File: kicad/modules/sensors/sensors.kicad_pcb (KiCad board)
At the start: 2 copper layers, 84.6 x 64 mm, 46 parts, among them J1 Bus_PCI_Express_x1, J2 TYPE-C-31-M-04, J3 Conn_01x02, U2 RP2040, U4 W25Q128JVP, U5 BMP388, U8 BNO055, U9 MCP25625T-E/ML, X1 ABM8-272-T3, Y1 ABS07-32.768KHZ-T, Y2 X322516MLB4SI

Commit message: begin routing
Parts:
- removed J3: Conn_01x02, Connector_PinHeader_2.54mm:PinHeader_1x02_P2.54mm_Vertical
- added J4: Conn_01x02, Connector_PinHeader_2.54mm:PinHeader_1x02_P2.54mm_Vertical, F.Cu at (122.0, 116.7)
- moved C10 93.2 mm to (148.5, 91.0)
- moved R12 91.0 mm to (146.3, 92.1), turned to 90 degrees
- moved C11 89.8 mm to (145.0, 90.5), turned to 180 degrees
- moved C207 80.9 mm to (59.5, 86.9)
- moved R220 76.9 mm to (59.5, 98.9)
- moved R221 76.9 mm to (59.5, 100.9)
- moved C211 73.1 mm to (59.5, 90.0)
- moved C212 73.1 mm to (59.5, 92.0)
- moved C213 73.1 mm to (59.5, 93.9)
- moved C214 73.1 mm to (59.5, 95.9)
- moved S1 55.7 mm to (161.0, 117.4), turned to 180 degrees
- moved S2 35.9 mm to (131.0, 117.0), turned to 180 degrees
- moved R203 34.7 mm to (146.0, 105.5), turned to 90 degrees
- moved R204 31.9 mm to (144.5, 105.5), turned to 90 degrees
- moved C210 30.7 mm to (142.0, 105.5), turned to -90 degrees
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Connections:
- net Net-(C11-Pad1) renamed /XOUT_pre
- S1 pad A: Net-(S1-PadA) -> GND
- S1 pad B: Net-(S1-PadA) -> GND
- S1 pad C: Net-(S1-PadC) -> /~{USB_BOOT_S}
- S1 pad D: Net-(S1-PadC) -> /~{USB_BOOT_S}
- S2 pad A: Net-(S2-PadA) -> GND
- S2 pad B: Net-(S2-PadA) -> GND
- S2 pad C: Net-(S2-PadC) -> /RUN
- S2 pad D: Net-(S2-PadC) -> /RUN
- U2 pad 24: unconnected-(U2-SWCLK-Pad24) -> /SWCLK
- U2 pad 25: unconnected-(U2-SWD-Pad25) -> /SWD
- U2 pad 26: unconnected-(U2-RUN-Pad26) -> /RUN
- U2 pad 51: unconnected-(U2-QSPI_SD3-Pad51) -> /QSPI_SD3
- U2 pad 53: unconnected-(U2-QSPI_SD0-Pad53) -> /QSPI_SD0
- U2 pad 54: unconnected-(U2-QSPI_SD2-Pad54) -> /QSPI_SD2
- U2 pad 55: unconnected-(U2-QSPI_SD1-Pad55) -> /QSPI_SD1
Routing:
- net /QSPI_SS: track 0.00 -> 19.6 mm
- net /QSPI_SD1: track 0.00 -> 17.0 mm
- net /QSPI_SD2: track 0.00 -> 15.5 mm
- net /XIN: track 0.00 -> 8.78 mm
- net +3.3V: track 0.00 -> 8.31 mm
- net /QSPI_SD3: track 0.00 -> 8.02 mm
- net +1.1V: track 0.00 -> 7.47 mm
- net /QSPI_SCLK: track 0.00 -> 7.09 mm
- net /QSPI_SD0: track 0.00 -> 6.17 mm
- net /XOUT_pre: track 0.00 -> 3.10 mm
- net /XOUT: track 0.00 -> 1.70 mm

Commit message: continue routing
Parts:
- moved R220 103.5 mm to (163.0, 100.5), turned to 180 degrees
- moved R221 93.5 mm to (153.0, 99.5), turned to 180 degrees
- moved C81 87.4 mm to (167.6, 88.1)
- moved C50 86.3 mm to (160.0, 97.0)
- moved C51 83.3 mm to (157.0, 98.5), turned to 180 degrees
- moved C82 82.6 mm to (162.6, 88.1)
- moved R87 80.6 mm to (159.0, 87.5), turned to 90 degrees
- moved C84 78.0 mm to (158.0, 91.0)
- moved D88 76.0 mm to (155.5, 92.5)
- moved R89 73.8 mm to (153.8, 94.0), turned to 180 degrees
- moved R83 72.7 mm to (153.1, 97.3), turned to 90 degrees
- moved Y1 50.0 mm to (169.7, 92.1)
- moved U8 37.3 mm to (162.8, 92.4), turned to -90 degrees
- moved U5 32.3 mm to (159.7, 99.0)
- moved Y2 31.5 mm to (139.2, 79.4), turned to 180 degrees
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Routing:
- net SDA: track 0.00 -> 22.1 mm
- net SCL: track 0.00 -> 21.6 mm
- net BOOT_LOAD: track 0.00 -> 19.7 mm
- net SO: track 0.00 -> 16.4 mm
- net BNORESET: track 0.00 -> 13.3 mm
- net BNOINT: track 0.00 -> 12.8 mm
- net +3.3V: track 8.31 -> 15.6 mm
- net OSC2: track 0.00 -> 6.82 mm
- net Net-(U8-XOUT32): track 0.00 -> 6.05 mm
- net Net-(U8-XIN32): track 0.00 -> 5.43 mm
- net Net-(D88-A): track 0.00 -> 4.95 mm
- net OSC1: track 0.00 -> 4.47 mm
- net Net-(U8-CAP): track 0.00 -> 2.87 mm
- net Net-(D88-K): track 0.00 -> 1.53 mm
- net /XOUT: track 1.70 -> 2.79 mm
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
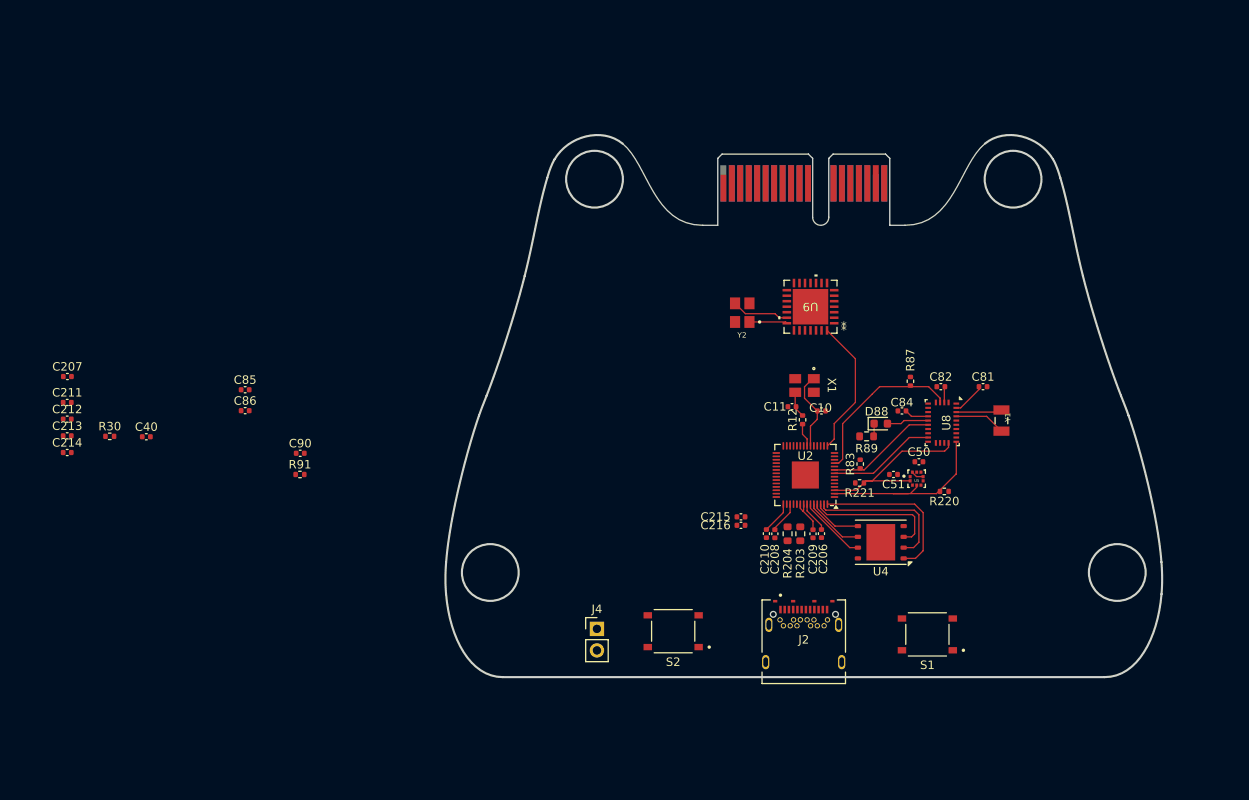
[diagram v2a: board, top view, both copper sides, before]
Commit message: finish most routing
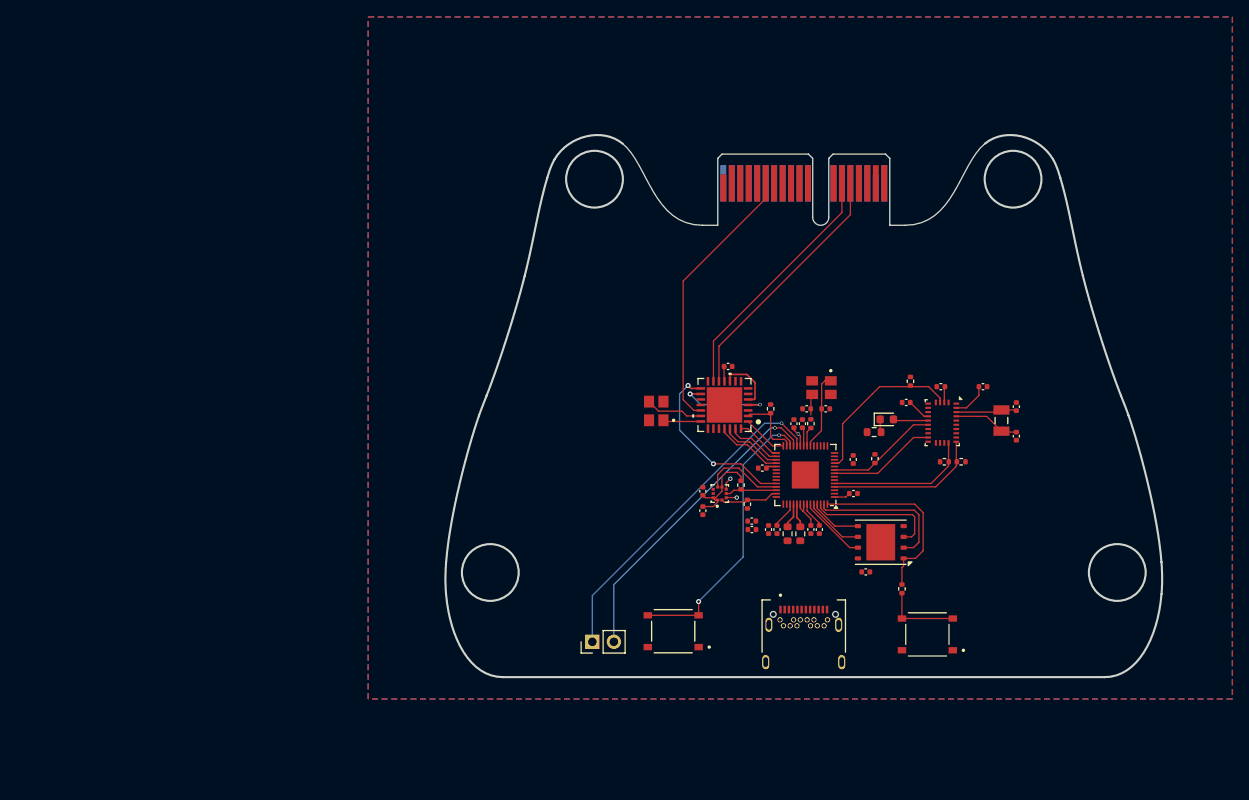
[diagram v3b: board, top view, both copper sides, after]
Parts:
- added R222: 4.7k, Resistor_SMD:R_0402_1005Metric, F.Cu at (139.8, 102.0)
- added R223: 4.7k, Resistor_SMD:R_0402_1005Metric, F.Cu at (139.0, 99.8)
- X1: footprint crystal:ABM8-272-T3_ABR -> ABM8-272-T3:ABM8-272-T3_ABR
- moved R30 95.2 mm to (158.0, 112.0), turned to -90 degrees
- moved C211 93.4 mm to (152.3, 100.8)
- moved C213 92.8 mm to (152.2, 96.7), turned to 90 degrees
- moved C85 91.2 mm to (171.5, 94.0), turned to -90 degrees
- moved C86 91.0 mm to (171.5, 90.5), turned to -90 degrees
- moved C214 86.8 mm to (146.2, 92.5), turned to 90 degrees
- moved C40 86.4 mm to (153.7, 110.0)
- moved C207 85.9 mm to (145.2, 92.5), turned to 90 degrees
- moved C212 82.2 mm to (141.5, 97.8), turned to 180 degrees
- moved R91 56.1 mm to (142.5, 90.8), turned to -90 degrees
- moved C90 51.5 mm to (137.5, 85.8)
- moved C50 26.1 mm to (134.5, 102.8), turned to -90 degrees
- moved U5 23.3 mm to (136.5, 100.8), turned to 90 degrees
- moved C51 22.6 mm to (134.5, 100.5), turned to 90 degrees
- moved Y2 15.4 mm to (129.0, 91.0)
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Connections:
- J1 pad A13: CANL -> CANH
- J1 pad A14: CANH -> CANL
- J1 pad B13: CANL -> CANH
- J1 pad B14: CANH -> CANL
- J2 pad A6: UDB_D+ -> USB_D+
- J2 pad A7: UDB_D- -> USB_D-
- J2 pad B6: UDB_D+ -> USB_D+
- J2 pad B7: UDB_D- -> USB_D-
- R203 pad 1: /USB_D+ -> USB_D+
- R204 pad 1: /USB_D- -> USB_D-
- R220 pad 1: +3V3 -> +3.3V
- R220 pad 2: SDA -> SDA1
- R221 pad 1: SCL -> SCL1
- R221 pad 2: +3V3 -> +3.3V
- U2 pad 14: SI -> unconnected-(U2-GPIO11-Pad14)
- U2 pad 15: SO -> unconnected-(U2-GPIO12-Pad15)
- U2 pad 16: CS -> unconnected-(U2-GPIO13-Pad16)
- U2 pad 17: SCK -> unconnected-(U2-GPIO14-Pad17)
- U2 pad 2: SDA -> unconnected-(U2-GPIO0-Pad2)
- U2 pad 27: CANSTBY -> CANRESET
- U2 pad 28: CANINT -> CS
- U2 pad 29: unconnected-(U2-GPIO18-Pad29) -> SO
- U2 pad 3: SCL -> unconnected-(U2-GPIO1-Pad3)
- U2 pad 30: unconnected-(U2-GPIO19-Pad30) -> SI
- U2 pad 31: unconnected-(U2-GPIO20-Pad31) -> SCK
- U2 pad 32: unconnected-(U2-GPIO21-Pad32) -> CANINT
- U2 pad 38: unconnected-(U2-GPIO26_ADC0-Pad38) -> CANSTBY
- U2 pad 39: unconnected-(U2-GPIO27_ADC1-Pad39) -> BMPINT
- U2 pad 4: unconnected-(U2-GPIO2-Pad4) -> SDA1
- U2 pad 40: unconnected-(U2-GPIO28_ADC2-Pad40) -> SDA0
- U2 pad 41: unconnected-(U2-GPIO29_ADC3-Pad41) -> SCL0
- U2 pad 5: BMPINT -> SCL1
- U5 pad 2: SCL -> SCL0
- U5 pad 4: SDA -> SDA0
- U8 pad 19: SCL -> SCL1
- U8 pad 20: SDA -> SDA1
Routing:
- net /SWCLK: track 0.00 -> 39.6 mm, vias 0 -> 1
- net /SWD: track 0.00 -> 36.9 mm, vias 0 -> 1
- net /RUN: track 0.00 -> 33.8 mm, vias 0 -> 2
- net +5V: track 0.00 -> 32.2 mm
- net CANL: track 0.00 -> 29.8 mm
- net CANH: track 0.00 -> 29.6 mm
- net SDA: track 22.1 -> 0.00 mm
- net SCL: track 21.6 -> 0.00 mm
- net CANSTBY: track 0.00 -> 21.3 mm, vias 0 -> 2
- net SDA1: track 0.00 -> 18.3 mm
- net SCL1: track 0.00 -> 17.0 mm
- net +3.3V: track 15.6 -> 27.8 mm
- net tx: track 0.00 -> 11.5 mm, vias 0 -> 2
- net SO: track 16.4 -> 5.35 mm
- net BMPINT: track 0.00 -> 9.62 mm
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- added copper zone on B.Cu, net GND
- added copper zone on F.Cu, net GND

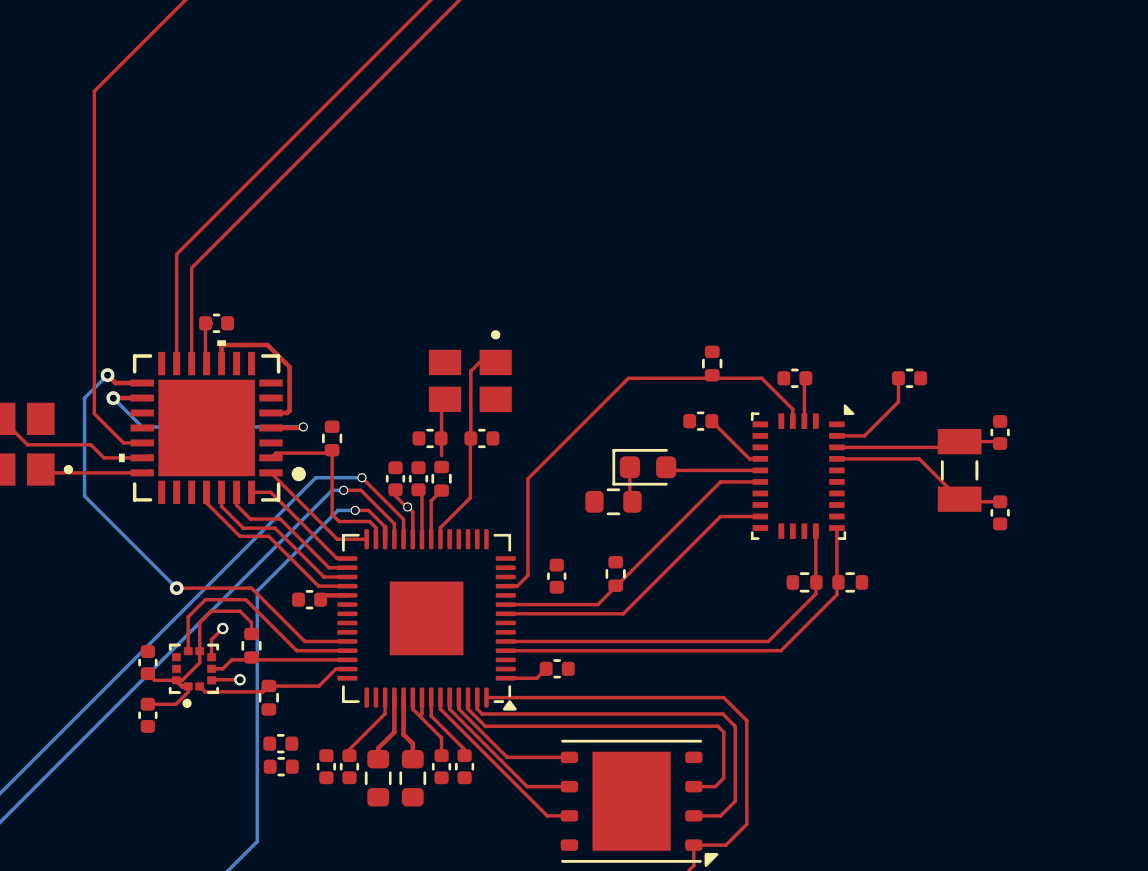
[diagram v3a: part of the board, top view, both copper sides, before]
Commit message: add new sensors, LDO and MOSFET
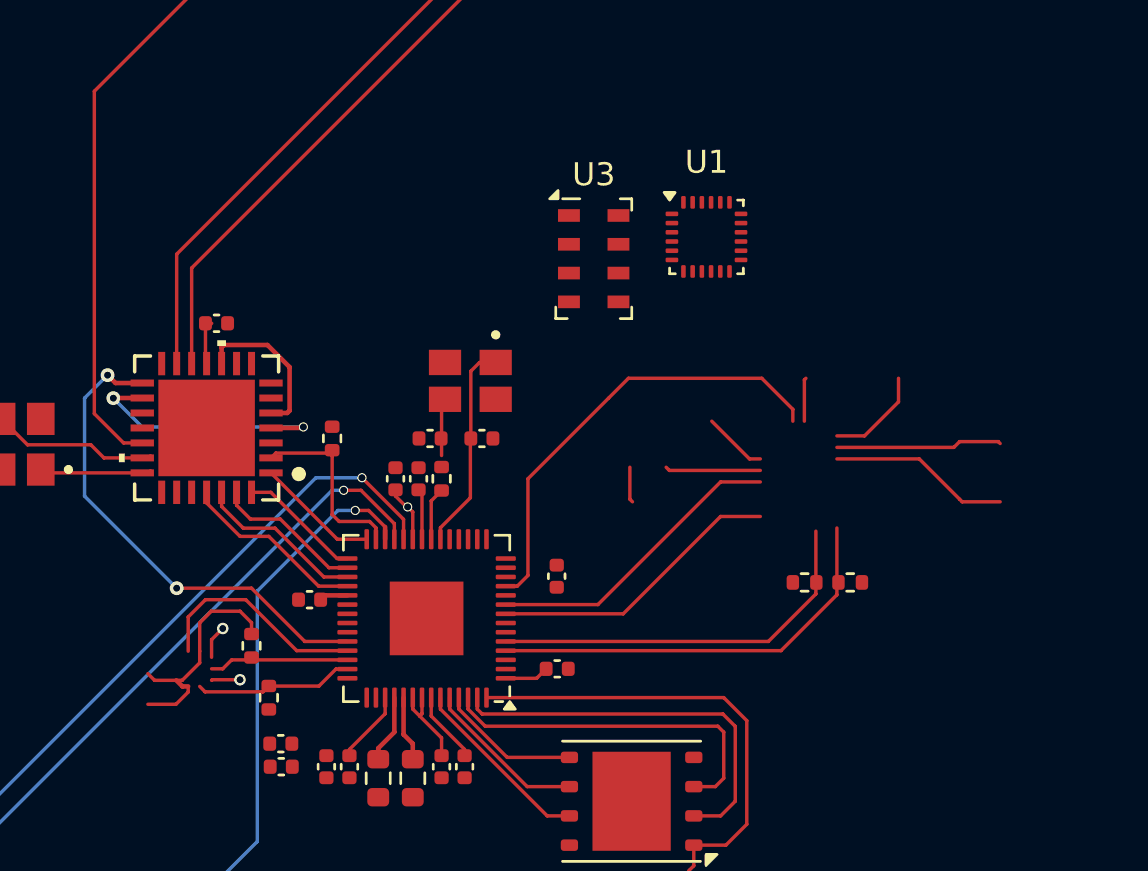
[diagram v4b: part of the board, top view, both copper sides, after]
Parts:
- removed C50, C51, C81, C82: 100n, Capacitor_SMD:C_0402_1005Metric
- removed C84: 1u, Capacitor_SMD:C_0402_1005Metric
- removed C85, C86: 22p, Capacitor_SMD:C_0402_1005Metric
- removed D88: LED, LED_SMD:LED_0603_1608Metric
- removed R83, R87: 10k, Resistor_SMD:R_0402_1005Metric
- removed R89: 150, Resistor_SMD:R_0603_1608Metric
- removed U5: BMP388, BMP388:PQFN50P200X200X80-10N
- removed U8: BNO055, Package_LGA:LGA-28_5.2x3.8mm_P0.5mm
- removed Y1: ABS07-32.768KHZ-T, ABS07-32.768KHZ-T:XTAL_ABS07-32.768KHZ-T
- added U1: ICM-20948, Sensor_Motion:InvenSense_QFN-24_3x3mm_P0.4mm, F.Cu at (158.8, 82.0)
- added U3: MS5607-02BA, Package_LGA:LGA-8_3x5mm_P1.25mm, F.Cu at (153.9, 82.9)
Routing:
- net (no net): track 0.00 -> 23.6 mm
- net Net-(U8-XOUT32): track 7.86 -> 0.00 mm
- net Net-(U8-XIN32): track 7.23 -> 0.00 mm
- net Net-(D88-A): track 4.14 -> 0.00 mm
- net Net-(U8-CAP): track 2.79 -> 0.00 mm
- net Net-(D88-K): track 1.55 -> 0.00 mm

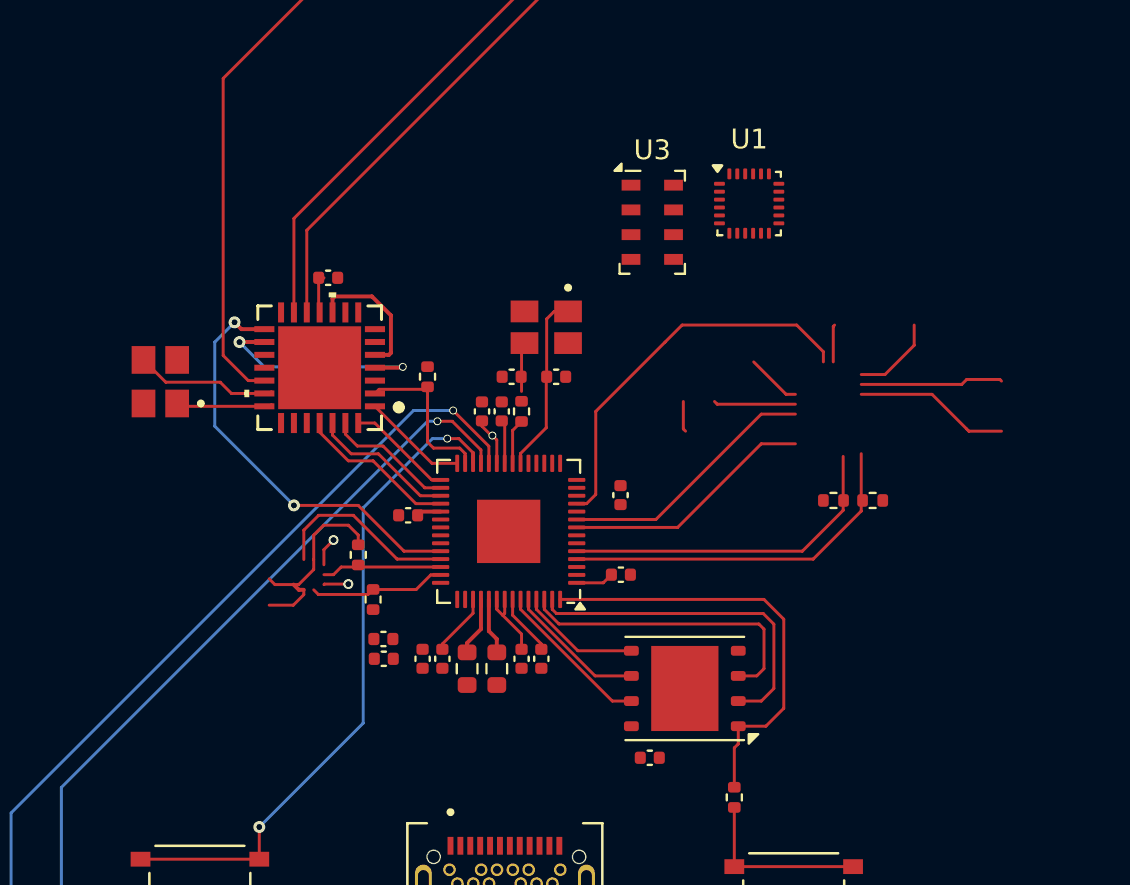
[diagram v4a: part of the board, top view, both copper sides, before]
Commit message: finish initial routing
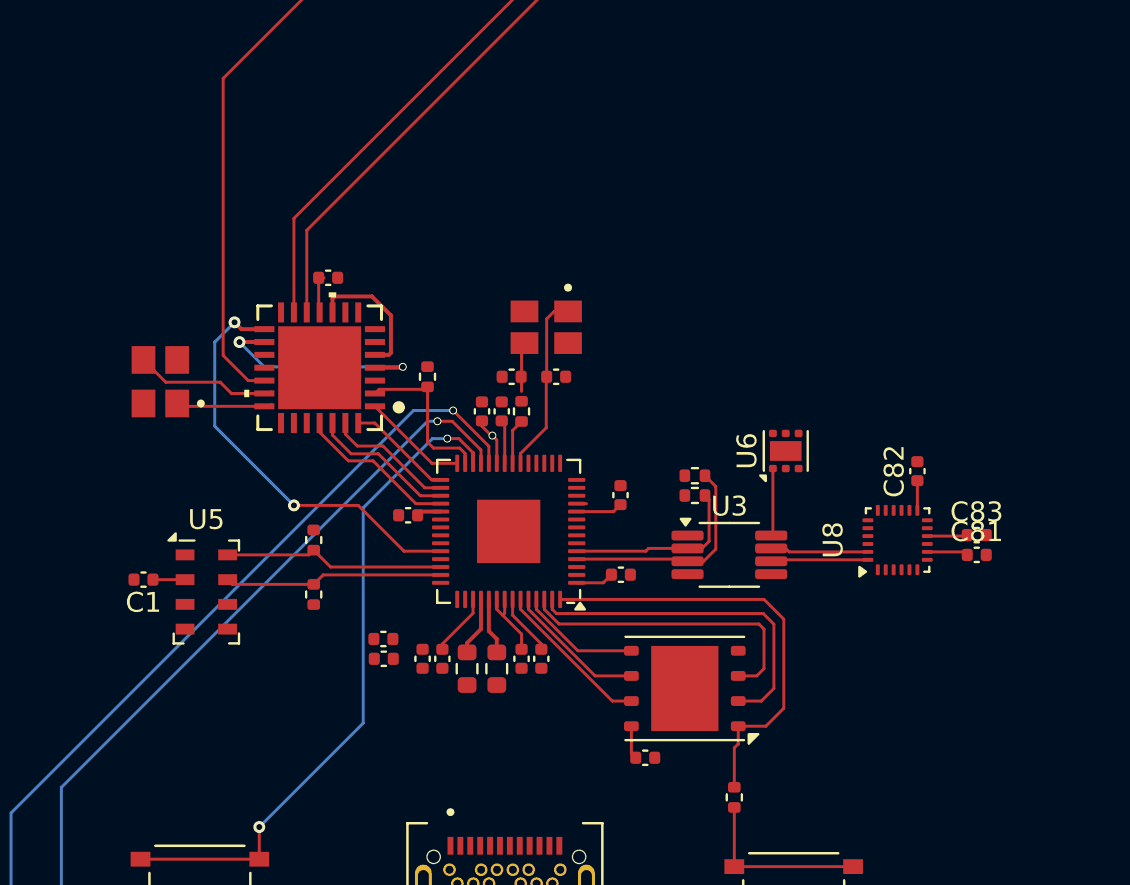
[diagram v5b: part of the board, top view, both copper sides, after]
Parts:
- removed U1: ICM-20948, Sensor_Motion:InvenSense_QFN-24_3x3mm_P0.4mm
- added C1: 100n, Capacitor_SMD:C_0402_1005Metric, F.Cu at (128.2, 101.0)
- added C81: 100n, Capacitor_SMD:C_0402_1005Metric, F.Cu at (170.2, 99.8)
- added C82: 100n, Capacitor_SMD:C_0402_1005Metric, F.Cu at (167.2, 95.5)
- added C83: 100n, Capacitor_SMD:C_0402_1005Metric, F.Cu at (170.2, 98.8)
- added U5: MS5607-02BA, Package_LGA:LGA-8_3x5mm_P1.25mm, F.Cu at (131.3, 101.6)
- added U6: TLV75718PDRV, Package_SON:WSON-6-1EP_2x2mm_P0.65mm_EP1x1.6mm, F.Cu at (160.6, 94.5)
- added U8: ICM-20948, Sensor_Motion:InvenSense_QFN-24_3x3mm_P0.4mm, F.Cu at (166.2, 99.0)
- U3: value MS5607-02BA -> TCA9803; footprint Package_LGA:LGA-8_3x5mm_P1.25mm -> Package_SO:VSSOP-8_3x3mm_P0.65mm
- moved U3 17.2 mm to (157.8, 99.7)
- moved R220 9.07 mm to (156.0, 95.8), turned to 0 degrees
- moved R221 7.00 mm to (156.0, 96.8)
- moved R222 3.01 mm to (136.8, 101.8)
- moved R223 2.37 mm to (136.8, 99.0)
- moved C40 0.23 mm to (153.5, 110.0)
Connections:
- R222 pad 1: SCL0 -> SDA0
- R223 pad 2: SDA0 -> SCL0
- U2 pad 11: BOOT_LOAD -> unconnected-(U2-GPIO8-Pad11)
- U2 pad 39: BMPINT -> unconnected-(U2-GPIO27_ADC1-Pad39)
- U2 pad 40: SDA0 -> SCL0
- U2 pad 41: SCL0 -> SDA0
- U2 pad 8: BNOINT -> unconnected-(U2-GPIO6-Pad8)
- U2 pad 9: BNORESET -> unconnected-(U2-GPIO7-Pad9)
- U3 pad 1: unconnected-(U3-VDD-Pad1) -> +3.3V
- U3 pad 2: unconnected-(U3-PS-Pad2) -> SCL1
- U3 pad 3: unconnected-(U3-GND-Pad3) -> SDA1
- U3 pad 4: Net-(U3-CSB-Pad4) -> GND
- U3 pad 5: Net-(U3-CSB-Pad4) -> +3.3V
- U3 pad 6: unconnected-(U3-SDO-Pad6) -> SDA1.8
- U3 pad 7: unconnected-(U3-SDI/SDA-Pad7) -> SCL1.8
- U3 pad 8: unconnected-(U3-SCLK-Pad8) -> +1.8V
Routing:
- net (no net): track 23.6 -> 0.00 mm
- net BOOT_LOAD: track 19.7 -> 0.00 mm
- net BNORESET: track 13.3 -> 0.00 mm
- net BNOINT: track 12.8 -> 0.00 mm
- net BMPINT: track 9.62 -> 0.00 mm
- net +3.3V: track 27.8 -> 18.3 mm
- net SCL1: track 17.0 -> 9.29 mm
- net SDA1: track 18.3 -> 11.3 mm
- net +1.8V: track 0.00 -> 5.50 mm
- net SDA0: track 6.06 -> 11.1 mm
- net SCL1.8: track 0.00 -> 4.96 mm
- net SDA1.8: track 0.00 -> 4.92 mm
- net SCL0: track 6.92 -> 11.2 mm
- net GND: track 2.85 -> 0.15 mm, vias 2 -> 0
- net Net-(U8-REGOUT): track 0.00 -> 2.12 mm
